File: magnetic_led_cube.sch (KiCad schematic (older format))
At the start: 7 parts, among them P1 CONN_01X02, P2 CONN_01X02, P3 CONN_01X02, P4 CONN_01X02

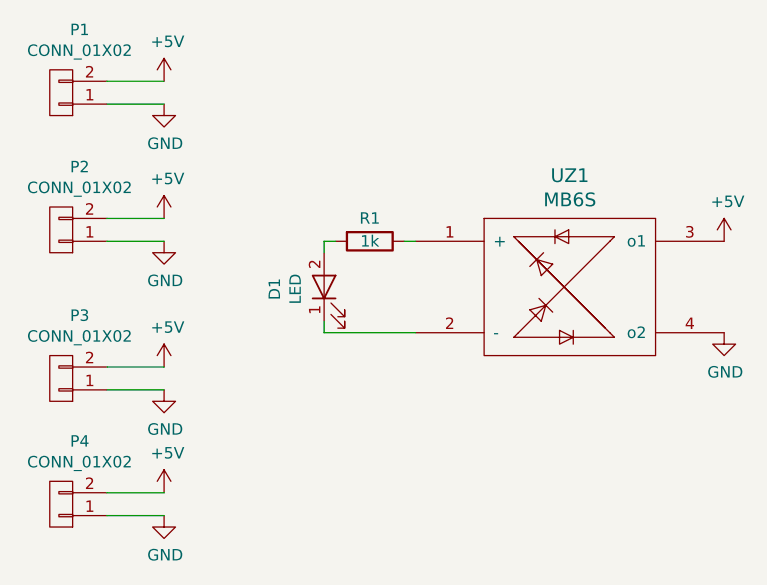
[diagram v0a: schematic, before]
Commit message: Complete maybe....
1. The mb6s library files for pcb, schematic have been added to lib dir.
2. Gerber files ares added to output dir. If I want to order new PCB to
pcb shop and I have to send that files.

[ticket: X]
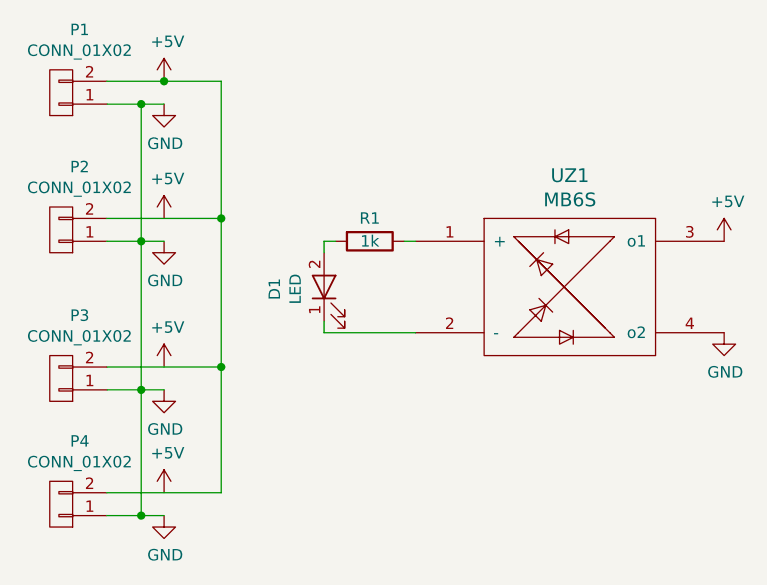
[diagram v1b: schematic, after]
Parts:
- R1: footprint (none) -> Resistors_THT:Resistor_Horizontal_RM7mm
- UZ1: footprint (none) -> mb6s:mb6s
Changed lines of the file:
@@
 LIBS:contrib
 LIBS:valves
+LIBS:magnetic_led_cube-cache
 EELAYER 26 0
 EELAYER END
@@
 $EndComp
 $Comp
-L +5V #PWR1
-U 1 1 584A3E71
-P 6750 1650
-F 0 "#PWR1" H 6750 1500 50  0001 C CNN
-F 1 "+5V" H 6765 1823 50  0000 C CNN
-F 2 "" H 6750 1650 50  0000 C CNN
-F 3 "" H 6750 1650 50  0000 C CNN
-	1    6750 1650
-	1    0    0    -1
-$EndComp
-$Comp
-L +5V #PWR3
-U 1 1 584A3E91
-P 6750 2250
-F 0 "#PWR3" H 6750 2100 50  0001 C CNN
-F 1 "+5V" H 6765 2423 50  0000 C CNN
-F 2 "" H 6750 2250 50  0000 C CNN
-F 3 "" H 6750 2250 50  0000 C CNN
-	1    6750 2250
-	1    0    0    -1
-$EndComp
-$Comp
-L +5V #PWR5
-U 1 1 584A3EB1
-P 6750 2900
-F 0 "#PWR5" H 6750 2750 50  0001 C CNN
-F 1 "+5V" H 6765 3073 50  0000 C CNN
-F 2 "" H 6750 2900 50  0000 C CNN
-F 3 "" H 6750 2900 50  0000 C CNN
-	1    6750 2900
-	1    0    0    -1
-$EndComp
-$Comp
-L +5V #PWR7
-U 1 1 584A3ED1
-P 6750 3450
-F 0 "#PWR7" H 6750 3300 50  0001 C CNN
-F 1 "+5V" H 6765 3623 50  0000 C CNN
-F 2 "" H 6750 3450 50  0000 C CNN
-F 3 "" H 6750 3450 50  0000 C CNN
-	1    6750 3450
-	1    0    0    -1
-$EndComp
-Wire Wire Line
-	6500 2250 6750 2250
-Wire Wire Line
-	6500 1650 6750 1650
-Wire Wire Line
-	6500 2900 6750 2900
-Wire Wire Line
-	6500 3450 6750 3450
-$Comp
-L GND #PWR2
-U 1 1 584A43A7
-P 6750 1750
-F 0 "#PWR2" H 6750 1500 50  0001 C CNN
-F 1 "GND" H 6755 1577 50  0000 C CNN
-F 2 "" H 6750 1750 50  0000 C CNN
-F 3 "" H 6750 1750 50  0000 C CNN
-	1    6750 1750
-	1    0    0    -1
-$EndComp
-$Comp
-L GND #PWR4
-U 1 1 584A43C7
-P 6750 2350
-F 0 "#PWR4" H 6750 2100 50  0001 C CNN
-F 1 "GND" H 6755 2177 50  0000 C CNN
-F 2 "" H 6750 2350 50  0000 C CNN
-F 3 "" H 6750 2350 50  0000 C CNN
-	1    6750 2350
-	1    0    0    -1
-$EndComp
-$Comp
-L GND #PWR6
-U 1 1 584A43E7
-P 6750 3000
-F 0 "#PWR6" H 6750 2750 50  0001 C CNN
-F 1 "GND" H 6755 2827 50  0000 C CNN
-F 2 "" H 6750 3000 50  0000 C CNN
-F 3 "" H 6750 3000 50  0000 C CNN
-	1    6750 3000
-	1    0    0    -1
-$EndComp
-$Comp
-L GND #PWR8
-U 1 1 584A4407
-P 6750 3550
-F 0 "#PWR8" H 6750 3300 50  0001 C CNN
-F 1 "GND" H 6755 3377 50  0000 C CNN
-F 2 "" H 6750 3550 50  0000 C CNN
-F 3 "" H 6750 3550 50  0000 C CNN
-	1    6750 3550
-	1    0    0    -1
-$EndComp
-Wire Wire Line
-	6500 1750 6750 1750
-Wire Wire Line
-	6500 2350 6750 2350
-Wire Wire Line
-	6500 3000 6750 3000
-Wire Wire Line
-	6500 3550 6750 3550
-$Comp
 L MB6S UZ1
 U 1 1 584A7003
@@
 F 0 "UZ1" H 8525 3037 60  0000 C CNN
 F 1 "MB6S" H 8525 2931 60  0000 C CNN
-F 2 "" H 8500 2550 60  0000 C CNN
+F 2 "mb6s:mb6s" H 8500 2550 60  0001 C CNN
 F 3 "" H 8500 2550 60  0000 C CNN
 	1    8500 2550
@@
 $EndComp
 $Comp
-L +5V #PWR9
+L +5V #PWR09
 U 1 1 584A70D3
 P 9200 2350
-F 0 "#PWR9" H 9200 2200 50  0001 C CNN
+F 0 "#PWR09" H 9200 2200 50  0001 C CNN
 F 1 "+5V" H 9215 2523 50  0000 C CNN
 F 2 "" H 9200 2350 50  0000 C CNN
@@
 $EndComp
 $Comp
-L GND #PWR10
+L GND #PWR010
 U 1 1 584A70F5
 P 9200 2750
-F 0 "#PWR10" H 9200 2500 50  0001 C CNN
+F 0 "#PWR010" H 9200 2500 50  0001 C CNN
 F 1 "GND" H 9205 2577 50  0000 C CNN
 F 2 "" H 9200 2750 50  0000 C CNN
@@
 	1    0    0    -1
 $EndComp
-Wire Wire Line
-	7450 2350 7450 2400
-Wire Wire Line
-	7450 2700 7450 2750
-Wire Wire Line
-	7450 2750 7850 2750
 $Comp
 L R R1
@@
 F 0 "R1" V 7550 2350 50  0000 C CNN
 F 1 "1k" V 7650 2350 50  0000 C CNN
-F 2 "" V 7580 2350 50  0000 C CNN
+F 2 "Resistors_THT:Resistor_Horizontal_RM7mm" V 7580 2350 50  0001 C CNN
 F 3 "" H 7650 2350 50  0000 C CNN
 	1    7650 2350
 	0    1    1    0
 $EndComp
+$Comp
+L +5V #PWR01
+U 1 1 584A3E71
+P 6750 1650
+F 0 "#PWR01" H 6750 1500 50  0001 C CNN
+F 1 "+5V" H 6765 1823 50  0000 C CNN
+F 2 "" H 6750 1650 50  0000 C CNN
+F 3 "" H 6750 1650 50  0000 C CNN
+	1    6750 1650
+	1    0    0    -1
+$EndComp
+$Comp
+L GND #PWR05
+U 1 1 584A43A7
+P 6750 1750
+F 0 "#PWR05" H 6750 1500 50  0001 C CNN
+F 1 "GND" H 6755 1577 50  0000 C CNN
+F 2 "" H 6750 1750 50  0000 C CNN
+F 3 "" H 6750 1750 50  0000 C CNN
+	1    6750 1750
+	1    0    0    -1
+$EndComp
+Connection ~ 6650 3000
+Wire Wire Line
+	6500 3550 6750 3550
+Connection ~ 6650 2350
+Wire Wire Line
+	6500 3000 6750 3000
+Connection ~ 6650 1750
+Wire Wire Line
+	6500 2350 6750 2350
+Wire Wire Line
+	6650 1750 6650 3550
+Connection ~ 7000 2900
+Wire Wire Line
+	7000 3450 6500 3450
+Connection ~ 7000 2250
+Wire Wire Line
+	7000 2900 6500 2900
+Connection ~ 6750 1650
+Wire Wire Line
+	7000 2250 6500 2250
+Wire Wire Line
+	7000 1650 7000 3450
+Wire Wire Line
+	6500 1650 7000 1650
+Wire Wire Line
+	7800 2350 7850 2350
 Wire Wire Line
 	7450 2350 7500 2350
 Wire Wire Line
-	7800 2350 7850 2350
+	7450 2750 7850 2750
+Wire Wire Line
+	7450 2700 7450 2750
+Wire Wire Line
+	7450 2350 7450 2400
+Wire Wire Line
+	6500 1750 6750 1750
+$Comp
+L +5V #PWR?
+U 1 1 584A8926
+P 6750 2250
+F 0 "#PWR?" H 6750 2100 50  0001 C CNN
+F 1 "+5V" H 6765 2423 50  0000 C CNN
+F 2 "" H 6750 2250 50  0000 C CNN
+F 3 "" H 6750 2250 50  0000 C CNN
+	1    6750 2250
+	1    0    0    -1
+$EndComp
+$Comp
+L +5V #PWR?
+U 1 1 584A8948
+P 6750 2900
+F 0 "#PWR?" H 6750 2750 50  0001 C CNN
+F 1 "+5V" H 6765 3073 50  0000 C CNN
+F 2 "" H 6750 2900 50  0000 C CNN
+F 3 "" H 6750 2900 50  0000 C CNN
+	1    6750 2900
+	1    0    0    -1
+$EndComp
+$Comp
+L +5V #PWR?
+U 1 1 584A896A
+P 6750 3450
+F 0 "#PWR?" H 6750 3300 50  0001 C CNN
+F 1 "+5V" H 6765 3623 50  0000 C CNN
+F 2 "" H 6750 3450 50  0000 C CNN
+F 3 "" H 6750 3450 50  0000 C CNN
+	1    6750 3450
+	1    0    0    -1
+$EndComp
+$Comp
+L GND #PWR?
+U 1 1 584A898C
+P 6750 2350
+F 0 "#PWR?" H 6750 2100 50  0001 C CNN
+F 1 "GND" H 6755 2177 50  0000 C CNN
+F 2 "" H 6750 2350 50  0000 C CNN
+F 3 "" H 6750 2350 50  0000 C CNN
+	1    6750 2350
+	1    0    0    -1
+$EndComp
+$Comp
+L GND #PWR?
+U 1 1 584A89AE
+P 6750 3000
+F 0 "#PWR?" H 6750 2750 50  0001 C CNN
+F 1 "GND" H 6755 2827 50  0000 C CNN
+F 2 "" H 6750 3000 50  0000 C CNN
+F 3 "" H 6750 3000 50  0000 C CNN
+	1    6750 3000
+	1    0    0    -1
+$EndComp
+$Comp
+L GND #PWR?
+U 1 1 584A89D0
+P 6750 3550
+F 0 "#PWR?" H 6750 3300 50  0001 C CNN
+F 1 "GND" H 6755 3377 50  0000 C CNN
+F 2 "" H 6750 3550 50  0000 C CNN
+F 3 "" H 6750 3550 50  0000 C CNN
+	1    6750 3550
+	1    0    0    -1
+$EndComp
+Connection ~ 6650 3550
 $EndSCHEMATC
